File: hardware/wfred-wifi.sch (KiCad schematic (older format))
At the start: 12 parts, among them K401 UART_ESP, K402 UART_AVR, P401 ESP_BOOTLOAD, U401 ESP-12E

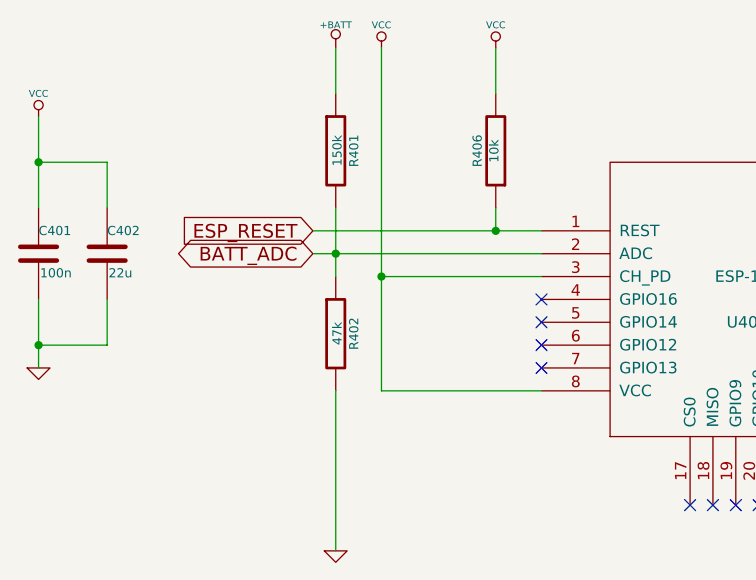
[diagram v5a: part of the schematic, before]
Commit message: Changed power concept (again)
- Exchanged regulator for one with lower shutdown current
- Moved AVR directly to battery
- Added voltage regulator enable connection to AVR
- Added Speed potentiometer power supply from AVR

New power concept: AVR stays always-on (POWER DOWN MODE if not in use)
and shuts down speed potentiometer and ESP8266 when idle or battery low
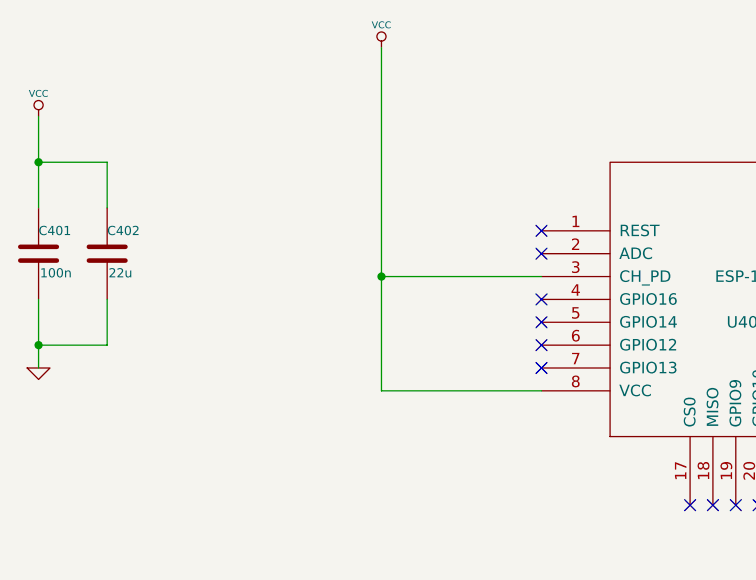
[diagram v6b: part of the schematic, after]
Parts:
- removed R401: 150k, Capacitors_SMD:C_0805_HandSoldering, symbol R-RESCUE-wfred_rev2
- removed R402: 47k, Capacitors_SMD:C_0805_HandSoldering, symbol R-RESCUE-wfred_rev2
- removed R406: 10k, Capacitors_SMD:C_0805_HandSoldering, symbol R-RESCUE-wfred_rev2
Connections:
- net BATT_ADC: no longer names the net of U401.2 (ADC)
- net ESP_RESET: no longer names the net of U401.1 (REST)
- no-connect marks 12 -> 14
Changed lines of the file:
@@
 LIBS:LDL1117S30R
 LIBS:MCP73831T-2ACI_OT
+LIBS:NCV8161BSN300T1G
 LIBS:wfred_rev2-cache
 EELAYER 25 0
@@
 	1    0    0    -1
 $EndComp
-$Comp
-L +BATT #PWR041
-U 1 1 5A11AB98
-P 2500 1500
-F 0 "#PWR041" H 2500 1450 20  0001 C CNN
-F 1 "+BATT" H 2500 1600 30  0000 C CNN
-F 2 "" H 2500 1500 60  0001 C CNN
-F 3 "" H 2500 1500 60  0001 C CNN
-	1    2500 1500
-	1    0    0    -1
-$EndComp
-Wire Wire Line
-	2500 1500 2500 1700
-$Comp
-L R-RESCUE-wfred_rev2 R401
-U 1 1 5A11AE00
-P 2500 1950
-F 0 "R401" V 2580 1950 40  0000 C CNN
-F 1 "150k" V 2507 1951 40  0000 C CNN
-F 2 "Capacitors_SMD:C_0805_HandSoldering" V 2430 1950 30  0001 C CNN
-F 3 "" H 2500 1950 30  0000 C CNN
-F 4 "603-RC0805JR-07100KL" V 2500 1950 60  0001 C CNN "Mouser"
-	1    2500 1950
-	1    0    0    -1
-$EndComp
-$Comp
-L R-RESCUE-wfred_rev2 R402
-U 1 1 5A11AE49
-P 2500 2750
-F 0 "R402" V 2580 2750 40  0000 C CNN
-F 1 "47k" V 2507 2751 40  0000 C CNN
-F 2 "Capacitors_SMD:C_0805_HandSoldering" V 2430 2750 30  0001 C CNN
-F 3 "" H 2500 2750 30  0000 C CNN
-F 4 "603-RC0805JR-07100KL" V 2500 2750 60  0001 C CNN "Mouser"
-	1    2500 2750
-	1    0    0    -1
-$EndComp
-Wire Wire Line
-	2500 2200 2500 2500
-Wire Wire Line
-	2400 2400 3400 2400
-Connection ~ 2500 2400
-$Comp
-L GND-RESCUE-wfred_rev2 #PWR042
-U 1 1 5A11B098
-P 2500 3700
-F 0 "#PWR042" H 2500 3700 30  0001 C CNN
-F 1 "GND" H 2500 3630 30  0001 C CNN
-F 2 "" H 2500 3700 60  0001 C CNN
-F 3 "" H 2500 3700 60  0001 C CNN
-	1    2500 3700
-	1    0    0    -1
-$EndComp
-Wire Wire Line
-	2500 3700 2500 3000
 NoConn ~ 4050 3500
 NoConn ~ 4150 3500
@@
 	1500 2800 1200 2800
 Connection ~ 1200 2800
-Text GLabel 2400 2400 0    60   BiDi ~ 0
-BATT_ADC
 NoConn ~ 5200 2500
 NoConn ~ 5200 2600
@@
 NoConn ~ 3400 2800
 NoConn ~ 3400 2900
-$Comp
-L R-RESCUE-wfred_rev2 R406
-U 1 1 5BDF6A62
-P 3200 1950
-F 0 "R406" V 3280 1950 40  0000 C CNN
-F 1 "10k" V 3207 1951 40  0000 C CNN
-F 2 "Capacitors_SMD:C_0805_HandSoldering" V 3130 1950 30  0001 C CNN
-F 3 "" H 3200 1950 30  0000 C CNN
-F 4 "603-RC0805JR-0710KL" V 3200 1950 60  0001 C CNN "Mouser"
-	1    3200 1950
-	-1   0    0    1
-$EndComp
-Wire Wire Line
-	3200 2200 3200 2300
-Wire Wire Line
-	2400 2300 3400 2300
-$Comp
-L VCC #PWR050
-U 1 1 5BDF6B6E
-P 3200 1500
-F 0 "#PWR050" H 3200 1600 30  0001 C CNN
-F 1 "VCC" H 3200 1600 30  0000 C CNN
-F 2 "" H 3200 1500 60  0001 C CNN
-F 3 "" H 3200 1500 60  0001 C CNN
-	1    3200 1500
-	1    0    0    -1
-$EndComp
-Wire Wire Line
-	3200 1500 3200 1700
-Text GLabel 2400 2300 0    60   Input ~ 0
-ESP_RESET
-Connection ~ 3200 2300
+NoConn ~ 3400 2400
+NoConn ~ 3400 2300
 $EndSCHEMATC
